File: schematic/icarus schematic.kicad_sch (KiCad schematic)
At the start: 49 parts, among them J2 USB_C_Receptacle_USB2.0_16P, M1 Motor_DC, M2 Motor_DC, M3 Motor_DC, M4 Motor_DC, Q1 AO3400A, Q2 AO3400A, Q3 AO3400A, Q4 AO3400A, SW1 SW_Push(BOOt), SW2 SW_Push(EN), U2 BMI088, U3 AMS1117-3.3, U4 ESP32-S3-WROOM-1

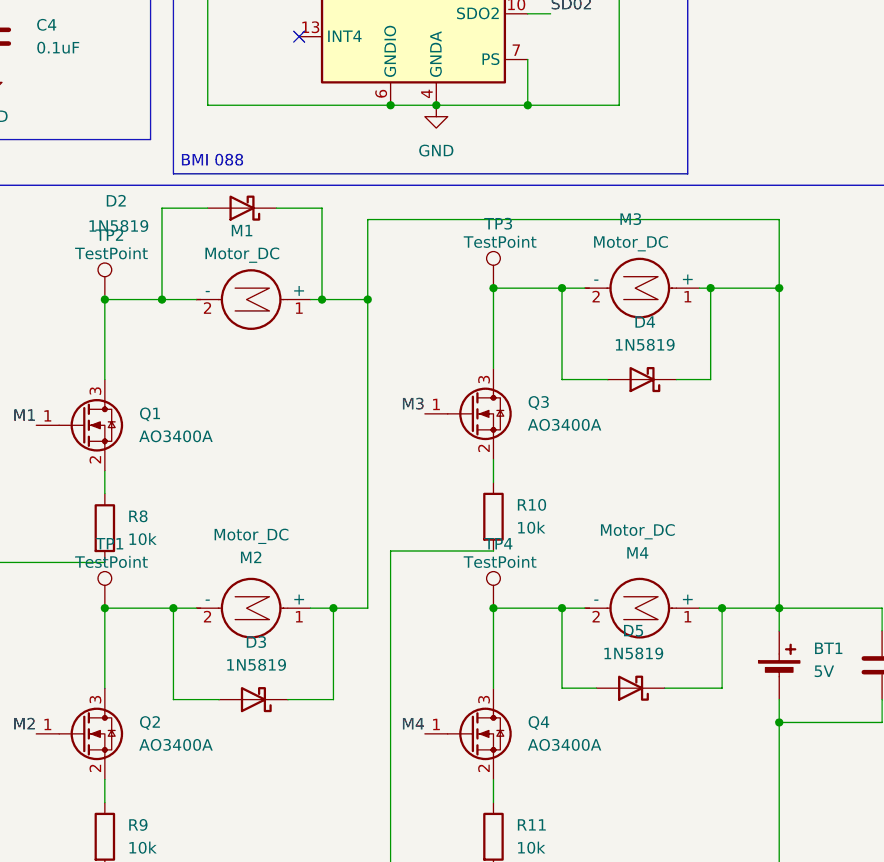
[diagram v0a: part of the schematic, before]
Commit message: Added capacitors across motors
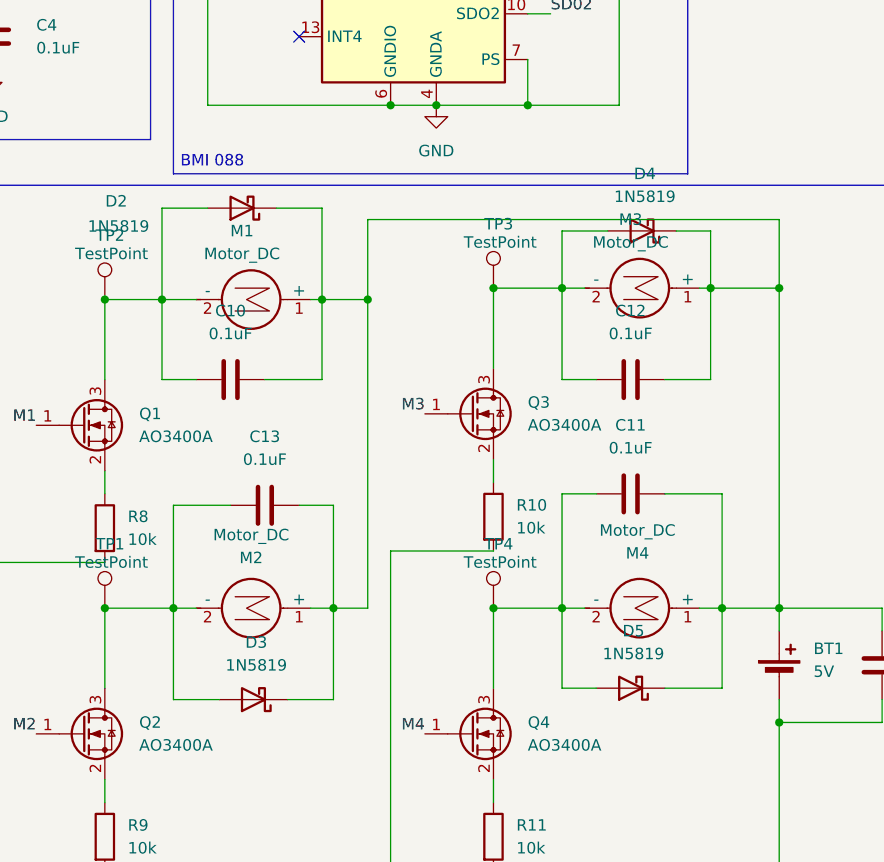
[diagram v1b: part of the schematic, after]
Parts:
- added C10, C11, C12, C13: 0.1uF, Capacitor_SMD:C_0603_1608Metric_Pad1.08x0.95mm_HandSolder, symbol Device:C
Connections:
- net at D2.2 (A), M1.2 (-), Q1.3 (D)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: now also C10.2
- net at BT1.1 (+), C8.1, D2.1 (K)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: now also C10.1, C11.1, C12.1, C13.1
- net at D5.2 (A), M4.2 (-), Q4.3 (D)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: now also C11.2
- net at D4.2 (A), M3.2 (-), Q3.3 (D)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: now also C12.2
- net at D3.2 (A), M2.2 (-), Q2.3 (D)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: now also C13.2
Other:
- moved on the sheet: D4

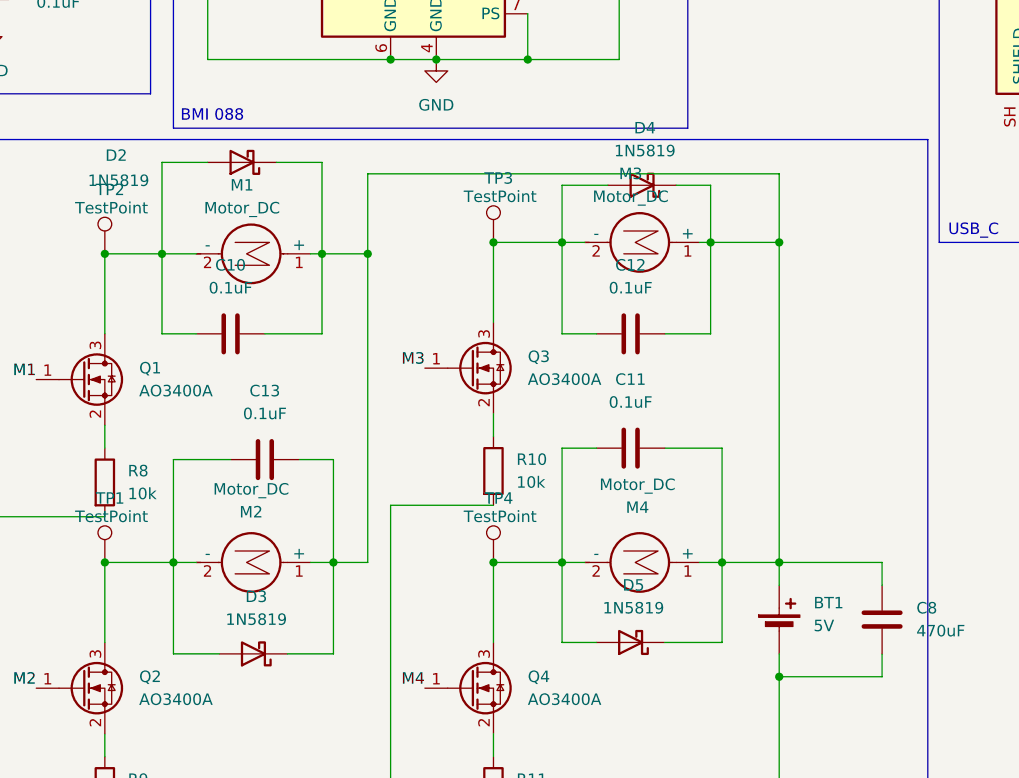
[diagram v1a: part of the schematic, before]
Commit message: Added connectors instead of motors.
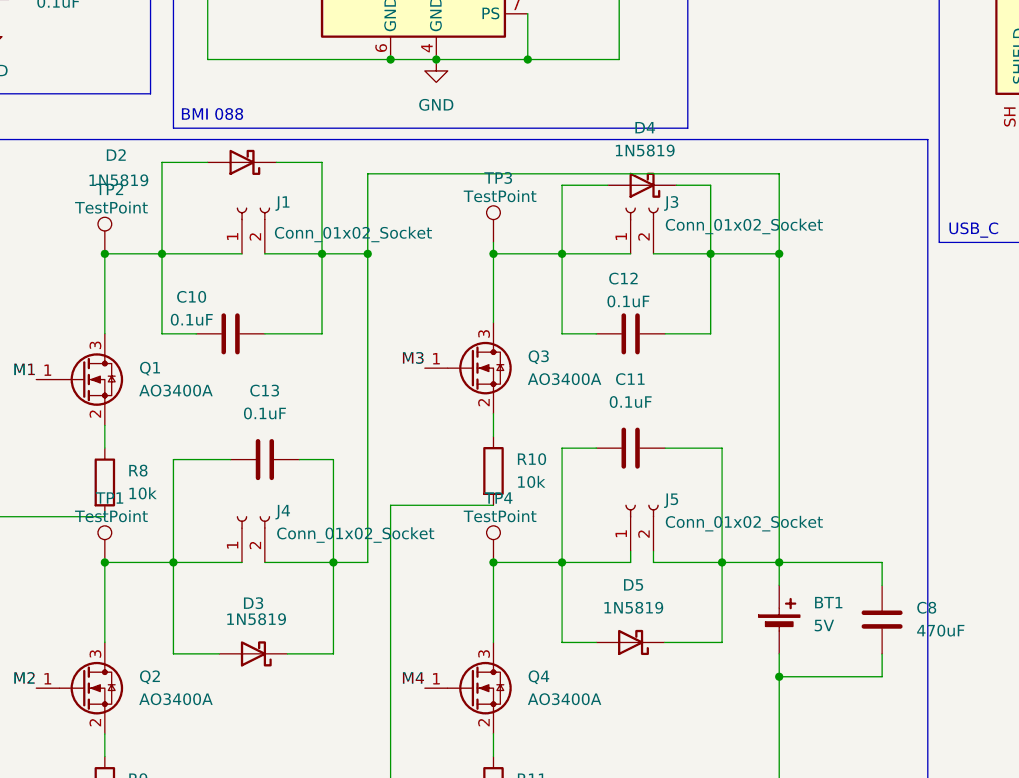
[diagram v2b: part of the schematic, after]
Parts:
- removed M1, M2, M3, M4: Motor_DC, Motors:Vybronics_VZ30C1T8219732L, symbol Motor:Motor_DC
- added J1, J3, J4, J5: Conn_01x02_Socket, Connector_JST:JST_EH_B2B-EH-A_1x02_P2.50mm_Vertical, symbol Connector:Conn_01x02_Socket
- BT1: footprint (none) -> Battery:BatteryHolder_Keystone_2460_1xAA
- C1, C3, C6, C7, C9: footprint Capacitor_SMD:C_0402_1005Metric -> Capacitor_SMD:C_0402_1005Metric_Pad0.74x0.62mm_HandSolder
- C4: footprint Capacitor_SMD:C_0805_2012Metric -> Capacitor_SMD:C_0402_1005Metric_Pad0.74x0.62mm_HandSolder
- C8: footprint Capacitor_SMD:C_0402_1005Metric_Pad0.74x0.62mm_HandSolder -> Capacitor_SMD:C_0603_1608Metric_Pad1.08x0.95mm_HandSolder
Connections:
- net at C10.2, D2.2 (A), Q1.3 (D)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: now also J1.1 (Pin_1)
- net at BT1.1 (+), C10.1, C11.1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: now also J1.2 (Pin_2), J3.2 (Pin_2), J4.2 (Pin_2), J5.2 (Pin_2)
- net at C11.2, D5.2 (A), Q4.3 (D)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: now also J5.1 (Pin_1)
- net at C12.2, D4.2 (A), Q3.3 (D)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: now also J3.1 (Pin_1)
- net at C13.2, D3.2 (A), Q2.3 (D)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: now also J4.1 (Pin_1)

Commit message: PCB first iteration.
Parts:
- removed BT1: 5V, Battery:BatteryHolder_Keystone_2460_1xAA, symbol Device:Battery_Cell
- added TP5, TP6: TestPoint, TestPoint:TestPoint_Pad_4.0x4.0mm, symbol Connector:TestPoint
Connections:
- net GND: now also TP6.1
- net at C10.1, C11.1, C12.1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: now also TP5.1
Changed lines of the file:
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@@
 	)
 	(symbol
-		(lib_id "Device:Battery_Cell")
-		(at 194.31 114.3 0)
-		(unit 1)
-		(body_style 1)
-		(exclude_from_sim no)
-		(in_bom yes)
-		(on_board yes)
-		(in_pos_files yes)
-		(dnp no)
-		(fields_autoplaced yes)
-		(property "Reference" "BT1"
-			(at 198.12 111.1884 0)
-			(show_name no)
-			(do_not_autoplace no)
-			(effects
-				(font
-					(size 1.27 1.27)
-				)
-				(justify left)
-			)
-		)
-		(property "Value" "5V"
-			(at 198.12 113.7284 0)
-			(show_name no)
-			(do_not_autoplace no)
-			(effects
-				(font
-					(size 1.27 1.27)
-				)
-				(justify left)
-			)
-		)
-		(property "Footprint" "Battery:BatteryHolder_Keystone_2460_1xAA"
-			(at 194.31 112.776 90)
-			(hide yes)
-			(show_name no)
-			(do_not_autoplace no)
-			(effects
-				(font
-					(size 1.27 1.27)
-				)
-			)
-		)
-		(property "Datasheet" ""
-			(at 194.31 112.776 90)
-			(hide yes)
-			(show_name no)
-			(do_not_autoplace no)
-			(effects
-				(font
-					(size 1.27 1.27)
-				)
-			)
-		)
-		(property "Description" "Single-cell battery"
-			(at 194.31 114.3 0)
-			(hide yes)
-			(show_name no)
-			(do_not_autoplace no)
-			(effects
-				(font
-					(size 1.27 1.27)
-				)
-			)
-		)
-		(property "Sim.Device" "V"
-			(at 194.31 114.3 0)
-			(hide yes)
-			(show_name no)
-			(do_not_autoplace no)
-			(effects
-				(font
-					(size 1.27 1.27)
-				)
-			)
-		)
-		(property "Sim.Type" "DC"
-			(at 194.31 114.3 0)
-			(hide yes)
-			(show_name no)
-			(do_not_autoplace no)
-			(effects
-				(font
-					(size 1.27 1.27)
-				)
-			)
-		)
-		(property "Sim.Pins" "1=+ 2=-"
-			(at 194.31 114.3 0)
-			(hide yes)
-			(show_name no)
-			(do_not_autoplace no)
-			(effects
-				(font
-					(size 1.27 1.27)
-				)
-			)
-		)
-		(pin "2"
-		)
-		(pin "1"
-		)
-		(instances
-			(project "icarus schematic"
-				(path "/7d2f9570-06fd-4dce-9677-8ff41db13bde"
-					(reference "BT1")
-					(unit 1)
-				)
-			)
-		)
-	)
-	(symbol
 		(lib_id "Device:R")
 		(at 247.65 29.21 90)
@@
 	)
 	(symbol
+		(lib_id "Connector:TestPoint")
+		(at 194.31 109.22 270)
+		(unit 1)
+		(body_style 1)
+		(exclude_from_sim no)
+		(in_bom yes)
+		(on_board yes)
+		(in_pos_files yes)
+		(dnp no)
+		(fields_autoplaced yes)
+		(property "Reference" "TP5"
+			(at 199.39 107.9499 90)
+			(show_name no)
+			(do_not_autoplace no)
+			(effects
+				(font
+					(size 1.27 1.27)
+				)
+				(justify left)
+			)
+		)
+		(property "Value" "TestPoint"
+			(at 199.39 110.4899 90)
+			(show_name no)
+			(do_not_autoplace no)
+			(effects
+				(font
+					(size 1.27 1.27)
+				)
+				(justify left)
+			)
+		)
+		(property "Footprint" "TestPoint:TestPoint_Pad_4.0x4.0mm"
+			(at 194.31 114.3 0)
+			(hide yes)
+			(show_name no)
+			(do_not_autoplace no)
+			(effects
+				(font
+					(size 1.27 1.27)
+				)
+			)
+		)
+		(property "Datasheet" ""
+			(at 194.31 114.3 0)
+			(hide yes)
+			(show_name no)
+			(do_not_autoplace no)
+			(effects
+				(font
+					(size 1.27 1.27)
+				)
+			)
+		)
+		(property "Description" "test point"
+			(at 194.31 109.22 0)
+			(hide yes)
+			(show_name no)
+			(do_not_autoplace no)
+			(effects
+				(font
+					(size 1.27 1.27)
+				)
+			)
+		)
+		(pin "1"
+		)
+		(instances
+			(project "icarus schematic"
+				(path "/7d2f9570-06fd-4dce-9677-8ff41db13bde"
+					(reference "TP5")
+					(unit 1)
+				)
+			)
+		)
+	)
+	(symbol
 		(lib_id "Device:R")
 		(at 162.56 96.52 0)
@@
 	)
 	(symbol
+		(lib_id "Connector:TestPoint")
+		(at 194.31 116.84 270)
+		(unit 1)
+		(body_style 1)
+		(exclude_from_sim no)
+		(in_bom yes)
+		(on_board yes)
+		(in_pos_files yes)
+		(dnp no)
+		(fields_autoplaced yes)
+		(property "Reference" "TP6"
+			(at 199.39 115.5699 90)
+			(show_name no)
+			(do_not_autoplace no)
+			(effects
+				(font
+					(size 1.27 1.27)
+				)
+				(justify left)
+			)
+		)
+		(property "Value" "TestPoint"
+			(at 199.39 118.1099 90)
+			(show_name no)
+			(do_not_autoplace no)
+			(effects
+				(font
+					(size 1.27 1.27)
+				)
+				(justify left)
+			)
+		)
+		(property "Footprint" "TestPoint:TestPoint_Pad_4.0x4.0mm"
+			(at 194.31 121.92 0)
+			(hide yes)
+			(show_name no)
+			(do_not_autoplace no)
+			(effects
+				(font
+					(size 1.27 1.27)
+				)
+			)
+		)
+		(property "Datasheet" ""
+			(at 194.31 121.92 0)
+			(hide yes)
+			(show_name no)
+			(do_not_autoplace no)
+			(effects
+				(font
+					(size 1.27 1.27)
+				)
+			)
+		)
+		(property "Description" "test point"
+			(at 194.31 116.84 0)
+			(hide yes)
+			(show_name no)
+			(do_not_autoplace no)
+			(effects
+				(font
+					(size 1.27 1.27)
+				)
+			)
+		)
+		(pin "1"
+		)
+		(instances
+			(project "icarus schematic"
+				(path "/7d2f9570-06fd-4dce-9677-8ff41db13bde"
+					(reference "TP6")
+					(unit 1)
+				)
+			)
+		)
+	)
+	(symbol
 		(lib_id "Device:LED")
 		(at 19.05 35.56 90)
@@
 		(in_pos_files yes)
 		(dnp no)
-		(fields_autoplaced yes)
 		(property "Reference" "C8"
-			(at 209.55 111.7599 0)
+			(at 207.01 106.68 0)
 			(show_name no)
 			(do_not_autoplace no)
@@
 		)
 		(property "Value" "470uF"
-			(at 209.55 114.2999 0)
+			(at 204.978 103.632 0)
 			(show_name no)
 			(do_not_autoplace no)

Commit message: Schematic change
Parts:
- C8: footprint Capacitor_SMD:C_0603_1608Metric_Pad1.08x0.95mm_HandSolder -> Capacitor_THT:C_Radial_D6.3mm_H5.0mm_P2.50mm
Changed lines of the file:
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@@
 			)
 		)
-		(property "Footprint" "Capacitor_SMD:C_0603_1608Metric_Pad1.08x0.95mm_HandSolder"
+		(property "Footprint" "Capacitor_THT:C_Radial_D6.3mm_H5.0mm_P2.50mm"
 			(at 206.7052 116.84 0)
 			(hide yes)

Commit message: Merge branch 'main' of https://github.com/Aryan2804/Icarus
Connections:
- net GND: now also Q1.2 (S), Q2.2 (S), Q3.2 (S), Q4.2 (S)
- net M1: now also R8.1
- net M2: now also R9.1
- net M3: now also R10.1
- net M4: now also R11.1

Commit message: kicad
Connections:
- net BOOT: no longer SW1.1
- net EN: no longer SW2.1
- net GND: now also SW1.1, SW2.1
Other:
- moved on the sheet: C2, C4
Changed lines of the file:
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@@
 	)
 	(junction
-		(at 106.68 38.1)
-		(diameter 0)
-		(color 0 0 0 0)
-	)
-	(junction
 		(at 243.84 34.29)
 		(diameter 0)
@@
 	)
 	(junction
-		(at 86.36 27.94)
-		(diameter 0)
-		(color 0 0 0 0)
-	)
-	(junction
 		(at 143.51 135.89)
 		(diameter 0)
@@
 	)
 	(junction
+		(at 86.36 44.45)
+		(diameter 0)
+		(color 0 0 0 0)
+	)
+	(junction
 		(at 162.56 106.68)
 		(diameter 0)
@@
 	)
 	(junction
+		(at 86.36 27.94)
+		(diameter 0)
+		(color 0 0 0 0)
+	)
+	(junction
 		(at 279.4 21.59)
 		(diameter 0)
@@
 	)
 	(junction
+		(at 106.68 44.45)
+		(diameter 0)
+		(color 0 0 0 0)
+	)
+	(junction
 		(at 151.13 135.89)
 		(diameter 0)
@@
 	)
 	(junction
-		(at 86.36 38.1)
-		(diameter 0)
-		(color 0 0 0 0)
-	)
-	(junction
 		(at 162.56 72.39)
 		(diameter 0)
@@
 	(wire
 		(pts
+			(xy 86.36 43.18) (xy 86.36 44.45)
+		)
+		(stroke
+			(width 0)
+			(type default)
+		)
+	)
+	(wire
+		(pts
 			(xy 125.73 81.28) (xy 125.73 72.39)
 		)
@@
 	(wire
 		(pts
-			(xy 95.25 38.1) (xy 106.68 38.1)
-		)
-		(stroke
-			(width 0)
-			(type default)
-		)
-	)
-	(wire
-		(pts
 			(xy 40.64 102.87) (xy 44.45 102.87)
 		)
@@
 	(wire
 		(pts
-			(xy 106.68 27.94) (xy 106.68 38.1)
+			(xy 74.93 36.83) (xy 74.93 44.45)
 		)
 		(stroke
@@
 	(wire
 		(pts
+			(xy 95.25 38.1) (xy 95.25 44.45)
+		)
+		(stroke
+			(width 0)
+			(type default)
+		)
+	)
+	(wire
+		(pts
 			(xy 111.76 128.27) (xy 111.76 135.89)
 		)
@@
 	(wire
 		(pts
+			(xy 74.93 44.45) (xy 86.36 44.45)
+		)
+		(stroke
+			(width 0)
+			(type default)
+		)
+	)
+	(wire
+		(pts
 			(xy 173.99 81.28) (xy 170.18 81.28)
 		)
@@
 	(wire
 		(pts
-			(xy 86.36 38.1) (xy 86.36 39.37)
+			(xy 86.36 27.94) (xy 86.36 35.56)
 		)
 		(stroke
@@
 	(wire
 		(pts
+			(xy 86.36 45.72) (xy 86.36 44.45)
+		)
+		(stroke
+			(width 0)
+			(type default)
+		)
+	)
+	(wire
+		(pts
 			(xy 182.88 64.77) (xy 186.69 64.77)
 		)
@@
 	(wire
 		(pts
+			(xy 106.68 44.45) (xy 106.68 43.18)
+		)
+		(stroke
+			(width 0)
+			(type default)
+		)
+	)
+	(wire
+		(pts
 			(xy 256.54 59.69) (xy 256.54 62.23)
 		)
@@
 	(wire
 		(pts
-			(xy 86.36 27.94) (xy 86.36 38.1)
+			(xy 95.25 44.45) (xy 106.68 44.45)
 		)
 		(stroke
@@
 	(wire
 		(pts
-			(xy 74.93 38.1) (xy 74.93 36.83)
-		)
-		(stroke
-			(width 0)
-			(type default)
-		)
-	)
-	(wire
-		(pts
 			(xy 170.18 93.98) (xy 170.18 106.68)
 		)
@@
 	(wire
 		(pts
-			(xy 74.93 38.1) (xy 86.36 38.1)
+			(xy 180.34 106.68) (xy 187.96 106.68)
 		)
 		(stroke
@@
 	(wire
 		(pts
-			(xy 180.34 106.68) (xy 187.96 106.68)
+			(xy 151.13 16.51) (xy 151.13 20.32)
 		)
 		(stroke
@@
 	(wire
 		(pts
-			(xy 151.13 16.51) (xy 151.13 20.32)
+			(xy 186.69 72.39) (xy 186.69 81.28)
 		)
 		(stroke
@@
 	(wire
 		(pts
-			(xy 186.69 72.39) (xy 186.69 81.28)
+			(xy 106.68 101.6) (xy 106.68 139.7)
 		)
 		(stroke
@@
 	(wire
 		(pts
-			(xy 106.68 101.6) (xy 106.68 139.7)
+			(xy 243.84 39.37) (xy 243.84 41.91)
 		)
 		(stroke
@@
 	(wire
 		(pts
-			(xy 243.84 39.37) (xy 243.84 41.91)
+			(xy 151.13 16.51) (xy 130.81 16.51)
 		)
 		(stroke
@@
 	(wire
 		(pts
-			(xy 151.13 16.51) (xy 130.81 16.51)
+			(xy 106.68 49.53) (xy 106.68 44.45)
 		)
 		(stroke
@@
 	(wire
 		(pts
-			(xy 106.68 38.1) (xy 106.68 39.37)
+			(xy 106.68 27.94) (xy 106.68 35.56)
 		)
 		(stroke
@@
 	(symbol
 		(lib_id "Device:C")
-		(at 106.68 43.18 0)
+		(at 106.68 39.37 0)
 		(unit 1)
 		(body_style 1)
@@
 		(fields_autoplaced yes)
 		(property "Reference" "C4"
-			(at 111.76 41.9099 0)
+			(at 111.76 38.0999 0)
 			(show_name no)
 			(do_not_autoplace no)
@@
 		)
 		(property "Value" "0.1uF"
-			(at 111.76 44.4499 0)
+			(at 111.76 40.6399 0)
 			(show_name no)
 			(do_not_autoplace no)
@@
 		)
 		(property "Footprint" "Capacitor_SMD:C_0402_1005Metric_Pad0.74x0.62mm_HandSolder"
-			(at 107.6452 46.99 0)
+			(at 107.6452 43.18 0)
 			(hide yes)
 			(show_name no)
@@
 		)
 		(property "Datasheet" ""
-			(at 106.68 43.18 0)
+			(at 106.68 39.37 0)
 			(hide yes)
 			(show_name no)
@@
 		)
 		(property "Description" "Unpolarized capacitor"
-			(at 106.68 43.18 0)
+			(at 106.68 39.37 0)
 			(hide yes)
 			(show_name no)
@@
 	(symbol
 		(lib_id "power:GND")
-		(at 106.68 46.99 0)
+		(at 106.68 49.53 0)
 		(unit 1)
 		(body_style 1)
@@
 		(fields_autoplaced yes)
 		(property "Reference" "#PWR08"
-			(at 106.68 53.34 0)
+			(at 106.68 55.88 0)
 			(hide yes)
 			(show_name no)
@@
 		)
 		(property "Value" "GND"
-			(at 106.68 52.07 0)
+			(at 106.68 54.61 0)
 			(show_name no)
 			(do_not_autoplace no)
@@
 		)
 		(property "Footprint" ""
-			(at 106.68 46.99 0)
+			(at 106.68 49.53 0)
 			(hide yes)
 			(show_name no)
@@
 		)
 		(property "Datasheet" ""
-			(at 106.68 46.99 0)
+			(at 106.68 49.53 0)
 			(hide yes)
 			(show_name no)
@@
 		)
 		(property "Description" "Power symbol creates a global label with name \"GND\" , ground"
-			(at 106.68 46.99 0)
+			(at 106.68 49.53 0)
 			(hide yes)
 			(show_name no)
@@
 	(symbol
 		(lib_id "power:GND")
-		(at 86.36 46.99 0)
+		(at 86.36 45.72 0)
 		(unit 1)
 		(body_style 1)
@@
 		(fields_autoplaced yes)
 		(property "Reference" "#PWR07"
-			(at 86.36 53.34 0)
+			(at 86.36 52.07 0)
 			(hide yes)
 			(show_name no)
@@
 		)
 		(property "Value" "GND"
-			(at 86.36 52.07 0)
+			(at 86.36 50.8 0)
 			(show_name no)
 			(do_not_autoplace no)
@@
 		)
 		(property "Footprint" ""
-			(at 86.36 46.99 0)
+			(at 86.36 45.72 0)
 			(hide yes)
 			(show_name no)
@@
 		)
 		(property "Datasheet" ""
-			(at 86.36 46.99 0)
+			(at 86.36 45.72 0)
 			(hide yes)
 			(show_name no)
@@
 		)
 		(property "Description" "Power symbol creates a global label with name \"GND\" , ground"
-			(at 86.36 46.99 0)
+			(at 86.36 45.72 0)
 			(hide yes)
 			(show_name no)
@@
 	(symbol
 		(lib_id "Device:C")
-		(at 86.36 43.18 0)
+		(at 86.36 39.37 0)
 		(unit 1)
 		(body_style 1)
@@
 		(fields_autoplaced yes)
 		(property "Reference" "C2"
-			(at 91.44 41.9099 0)
+			(at 91.44 38.0999 0)
 			(show_name no)
 			(do_not_autoplace no)
@@
 		)
 		(property "Value" "0.1uF"
-			(at 91.44 44.4499 0)
+			(at 91.44 40.6399 0)
 			(show_name no)
 			(do_not_autoplace no)
@@
 		)
 		(property "Footprint" "Capacitor_SMD:C_0402_1005Metric_Pad0.74x0.62mm_HandSolder"
-			(at 87.3252 46.99 0)
+			(at 87.3252 43.18 0)
 			(hide yes)
 			(show_name no)
@@
 		)
 		(property "Datasheet" ""
-			(at 86.36 43.18 0)
+			(at 86.36 39.37 0)
 			(hide yes)
 			(show_name no)
@@
 		)
 		(property "Description" "Unpolarized capacitor"
-			(at 86.36 43.18 0)
+			(at 86.36 39.37 0)
 			(hide yes)
 			(show_name no)
